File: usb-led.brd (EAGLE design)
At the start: 41.9 x 12 mm, 13 parts, among them U1 Tiny85-20-SMT

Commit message: v0.0.0.1: ground plane
Added vRestrict over USB area.
Rerouted without ground planes, then readded.
Added board images and lists.
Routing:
- net USB_D_MINUS: track 12.6 -> 31.7 mm, vias 2 -> 0
- net MOSI/DIN: track 26.5 -> 20.6 mm
- net RESET: track 20.6 -> 25.0 mm, vias 1 -> 0
- net SCK: track 19.3 -> 22.4 mm
- net USB_D_MINUS_RAW: track 18.6 -> 21.4 mm
- net VCC: track 80.9 -> 78.5 mm, vias 3 -> 4
- net USB_D_PLUS_RAW: track 18.6 -> 20.8 mm
- net GND: track 87.5 -> 89.7 mm
- added copper zone on layer 1, net GND
- added copper zone on layer 16, net GND
- removed copper zone on layer 1, net N$2
- removed copper zone on layer 16, net N$3
- removed copper zone on layer 1, net N$4
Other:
- board text added: "v0.0.0.1"
- board text removed: "v0.0.1"

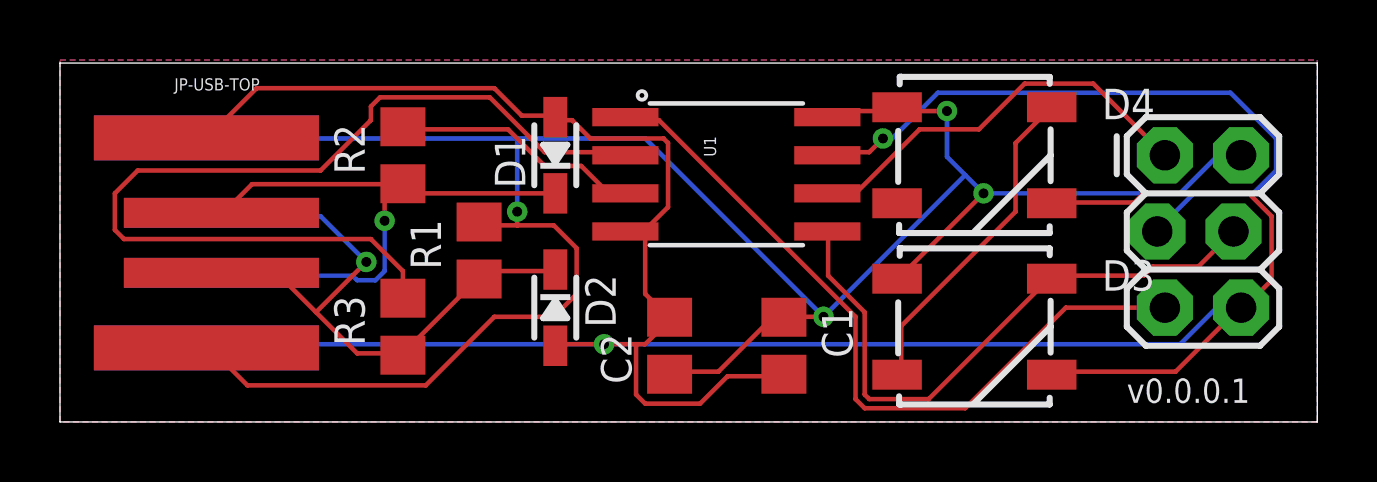
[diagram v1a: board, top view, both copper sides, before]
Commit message: Depend on SOIC clip. Add MacroFab dependencies (micro USB).
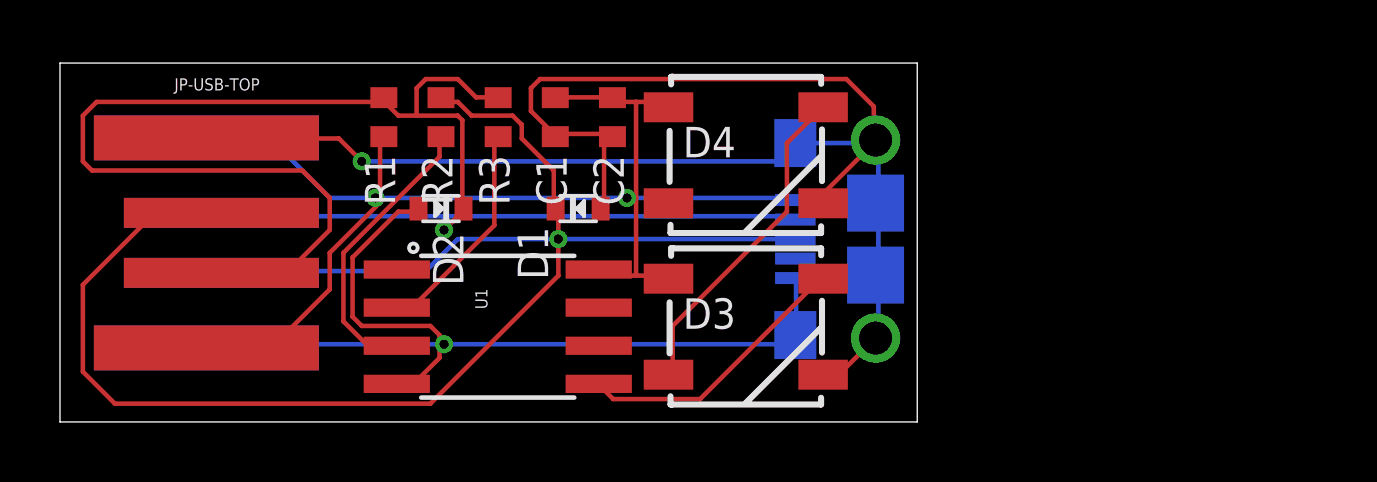
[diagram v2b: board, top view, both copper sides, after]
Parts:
- removed JP-ISP: AVR_SPI_PRG_62X3_LOCK, SparkFun-Connectors:2X3_LOCK
- added J1: (no value), MF_Connectors:MICROUSB-RIGHT
- C1: device rcl:C0805 -> rcl:C0402
- C2: value 1uF -> 0.1uF; device rcl:C0805 -> rcl:C0402
- D1, D2: value 3.6 -> 3.6V; device microbuilder:SOD-323 -> microbuilder:SOD-523
- R1: value 1K5 -> 1.5K; device rcl:R0805 -> rcl:R0402
- R2, R3: device rcl:R0805 -> rcl:R0402
- U1: value Tiny85-20-SMT -> ATtiny85-20SU
- moved C1 10.8 mm to (16.5, 10.2)
- moved U1 9.16 mm to (14.6, 3.17)
- moved C2 7.85 mm to (18.4, 10.2), turned to 270 degrees
- moved R3 7.67 mm to (14.6, 10.2), turned to 270 degrees
- moved D3 7.62 mm to (22.9, 3.17)
- moved D4 7.62 mm to (22.9, 8.89)
- moved R1 5.46 mm to (10.8, 10.2), turned to 270 degrees
- moved D2 5.04 mm to (12.7, 7.11)
- moved D1 1.93 mm to (17.3, 7.11)
- moved R2 1.80 mm to (12.7, 10.2), turned to 270 degrees
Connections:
- net GND: now also J1.5, J1.S1, J1.S2, J1.S3, J1.S4, J1.S5, J1.S6; no longer JP-ISP.6
- net MISO: no longer JP-ISP.1
- net MOSI/DIN: no longer JP-ISP.4
- net RESET: no longer JP-ISP.5
- net SCK: no longer JP-ISP.3
- net USB_D_MINUS_RAW: now also D2.K, J1.2; no longer D2.C
- net USB_D_PLUS_RAW: now also D1.K, J1.3; no longer D1.C
- net VCC: now also J1.1; no longer JP-ISP.2
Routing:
- net USB_D_MINUS_RAW: track 21.4 -> 56.4 mm
- net VCC: track 78.5 -> 44.0 mm, vias 4 -> 2
- net USB_D_PLUS_RAW: track 20.8 -> 54.8 mm
- net RESET: track 25.0 -> 0.00 mm
- net USB_D_MINUS: track 31.7 -> 7.42 mm
- net SCK: track 22.4 -> 0.00 mm, vias 1 -> 0
- net MISO: track 13.8 -> 0.00 mm
- net MOSI/DIN: track 20.6 -> 9.35 mm
- net USB_D_PLUS: track 8.39 -> 9.61 mm
- net GND: vias 1 -> 2
- removed copper zone on layer 1, net GND
- removed copper zone on layer 16, net GND
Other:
- board size 41.9 x 12 mm -> 28.6 x 12 mm
- board text added: "mike@sowbug.com"
- board text added: "version 1"
- board text removed: "v0.0.0.1"

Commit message: mf2.
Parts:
- removed J1: (no value), MF_Connectors:MICROUSB-RIGHT
- added JP-ISP: AVR_MINI_PROGSMD, SparkFun-Connectors:AVR_MINI_PROG
- added JP-USB-MICRO: (no value), MF_Connectors:MICROUSB-RIGHT
- moved C1 8.13 mm to (21.6, 3.81)
- moved C2 4.07 mm to (21.6, 7.62)
- moved D3 3.18 mm to (26.0, 3.17)
- moved D4 3.18 mm to (26.0, 8.89)
- moved D2 3.11 mm to (15.7, 7.75), turned to 0 degrees
- moved R3 2.84 mm to (13.3, 7.62), turned to 90 degrees
- moved D1 2.74 mm to (14.6, 7.75), turned to 180 degrees
- moved R2 0.63 mm to (12.1, 10.2)
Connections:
- net GND: now also JP-ISP.2, JP-USB-MICRO.5, JP-USB-MICRO.S1, JP-USB-MICRO.S2, JP-USB-MICRO.S3, JP-USB-MICRO.S4, JP-USB-MICRO.S5, JP-USB-MICRO.S6; no longer J1.5, J1.S1, J1.S2, J1.S3, J1.S4, J1.S5, J1.S6
- net MISO: now also JP-ISP.6
- net MOSI/DIN: now also JP-ISP.4
- net RESET: now also JP-ISP.3
- net SCK: now also JP-ISP.5
- net USB_D_MINUS_RAW: now also JP-USB-MICRO.2; no longer J1.2
- net USB_D_PLUS_RAW: now also JP-USB-MICRO.3; no longer J1.3
- net VCC: now also JP-ISP.1, JP-USB-MICRO.1; no longer J1.1
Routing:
- net VCC: track 44.0 -> 79.4 mm, vias 2 -> 1
- net GND: track 89.7 -> 117.2 mm, vias 2 -> 0
- net MOSI/DIN: track 9.35 -> 30.0 mm, vias 0 -> 1
- net USB_D_PLUS_RAW: track 54.8 -> 37.4 mm, vias 1 -> 2
- net USB_D_MINUS_RAW: track 56.4 -> 40.7 mm, vias 1 -> 4
- net RESET: track 0.00 -> 10.8 mm
- net MISO: track 0.00 -> 10.1 mm
- net SCK: track 0.00 -> 8.10 mm
- net USB_D_PLUS: track 9.61 -> 11.7 mm, vias 0 -> 2
- net USB_D_MINUS: track 7.42 -> 8.13 mm
- added copper zone on layer 1, net GND
- added copper zone on layer 16, net GND
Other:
- board size 28.6 x 12 mm -> 31.8 x 12 mm
- board text added: "version mf2"
- board text removed: "version 1"
